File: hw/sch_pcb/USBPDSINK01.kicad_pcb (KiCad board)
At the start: 2 copper layers, 45.5 x 52.9 mm, 53 parts, among them J1 USBC_USB4105-GF-A, J2 HEADER_2x05_PARALLEL, J3 HEADER_2x04_PARALLEL, J4 HEADER_2x03_PARALLEL, J5 HEADER_2x01, J6 HEADER_2x07_PARALLEL, J7 WAGO_2604-3102, M1 HOLE, M2 HOLE, M3 HOLE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

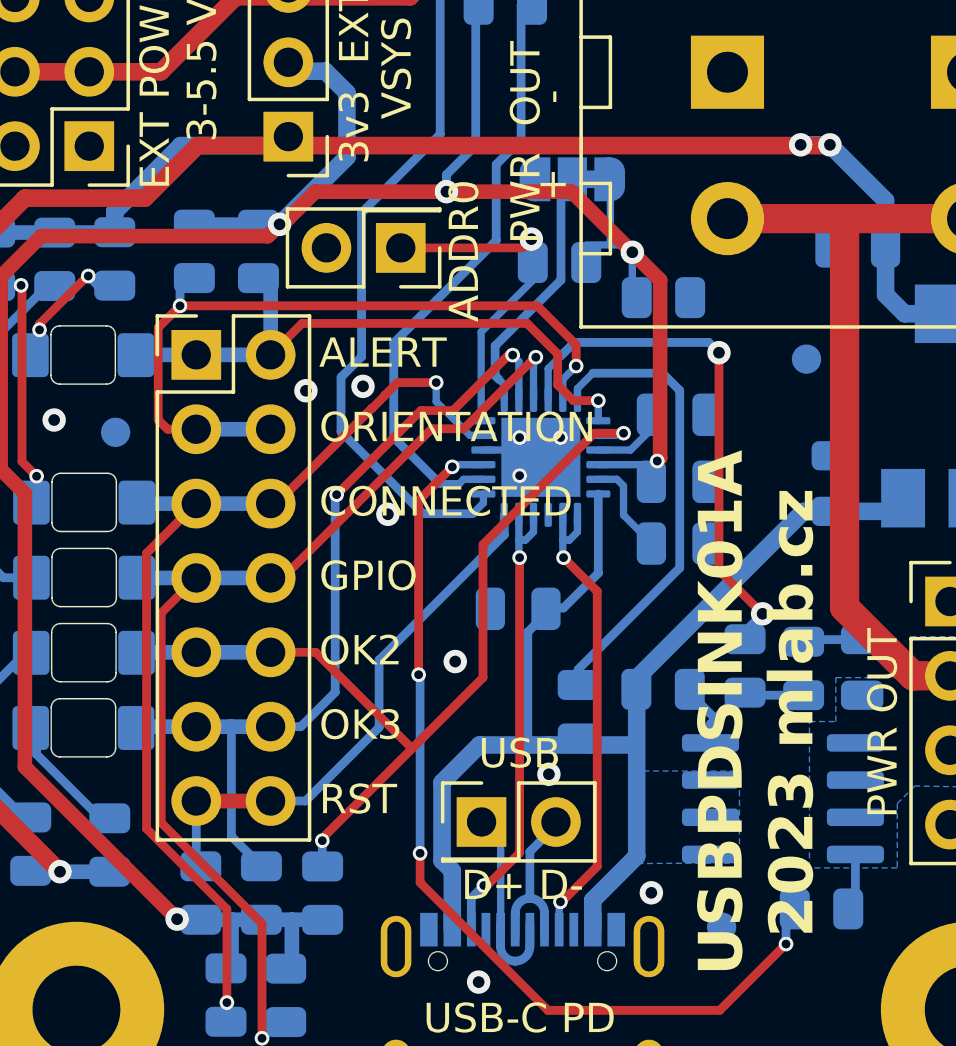
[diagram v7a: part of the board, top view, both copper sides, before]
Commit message: Cleanup traces.
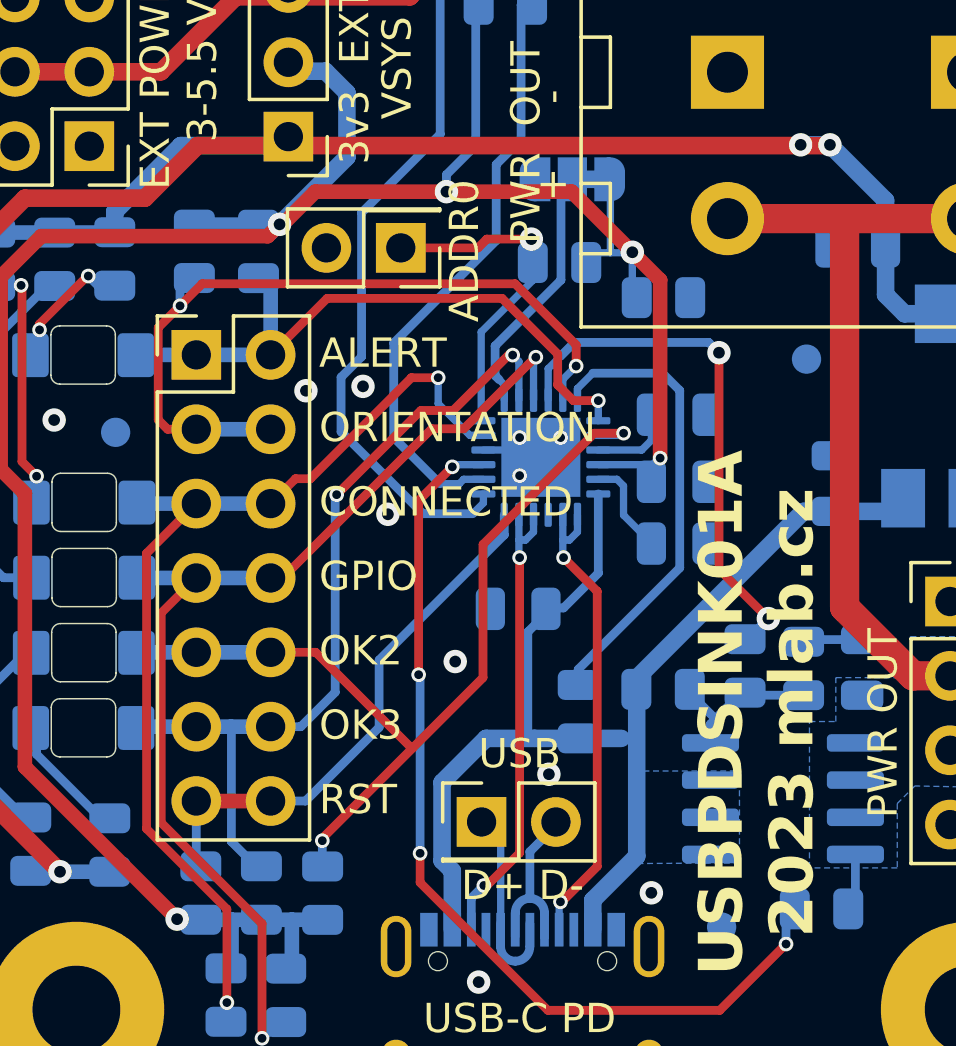
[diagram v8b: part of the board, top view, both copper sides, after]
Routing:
- net /ALERT: track 21.0 -> 21.8 mm
- net /SIDE: track 25.0 -> 25.6 mm
